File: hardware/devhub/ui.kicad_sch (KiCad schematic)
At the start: 12 parts, among them U10 74HC595, U11 74HC595

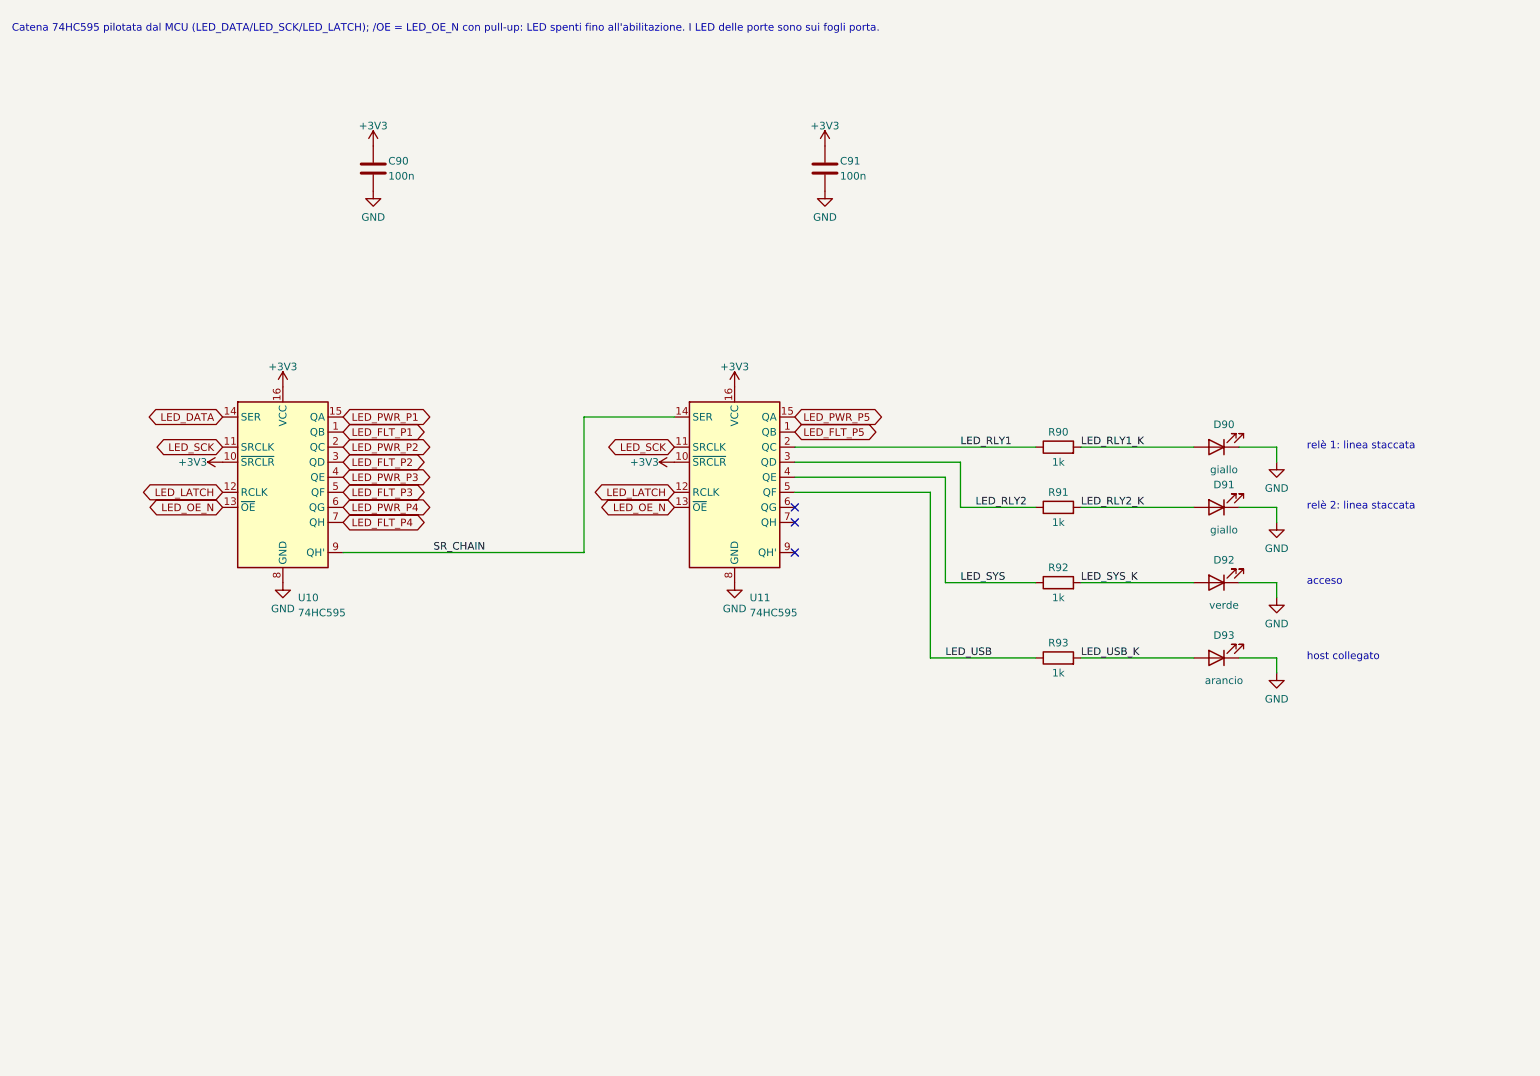
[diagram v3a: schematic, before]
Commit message: Simplification: drop the 74HC595s, green LEDs on port EN, relay LEDs on relay commands (D38)
Red port LEDs and the host LED are driven by GPIOs that stay low in DFU; the power LED is on 3.3 V.
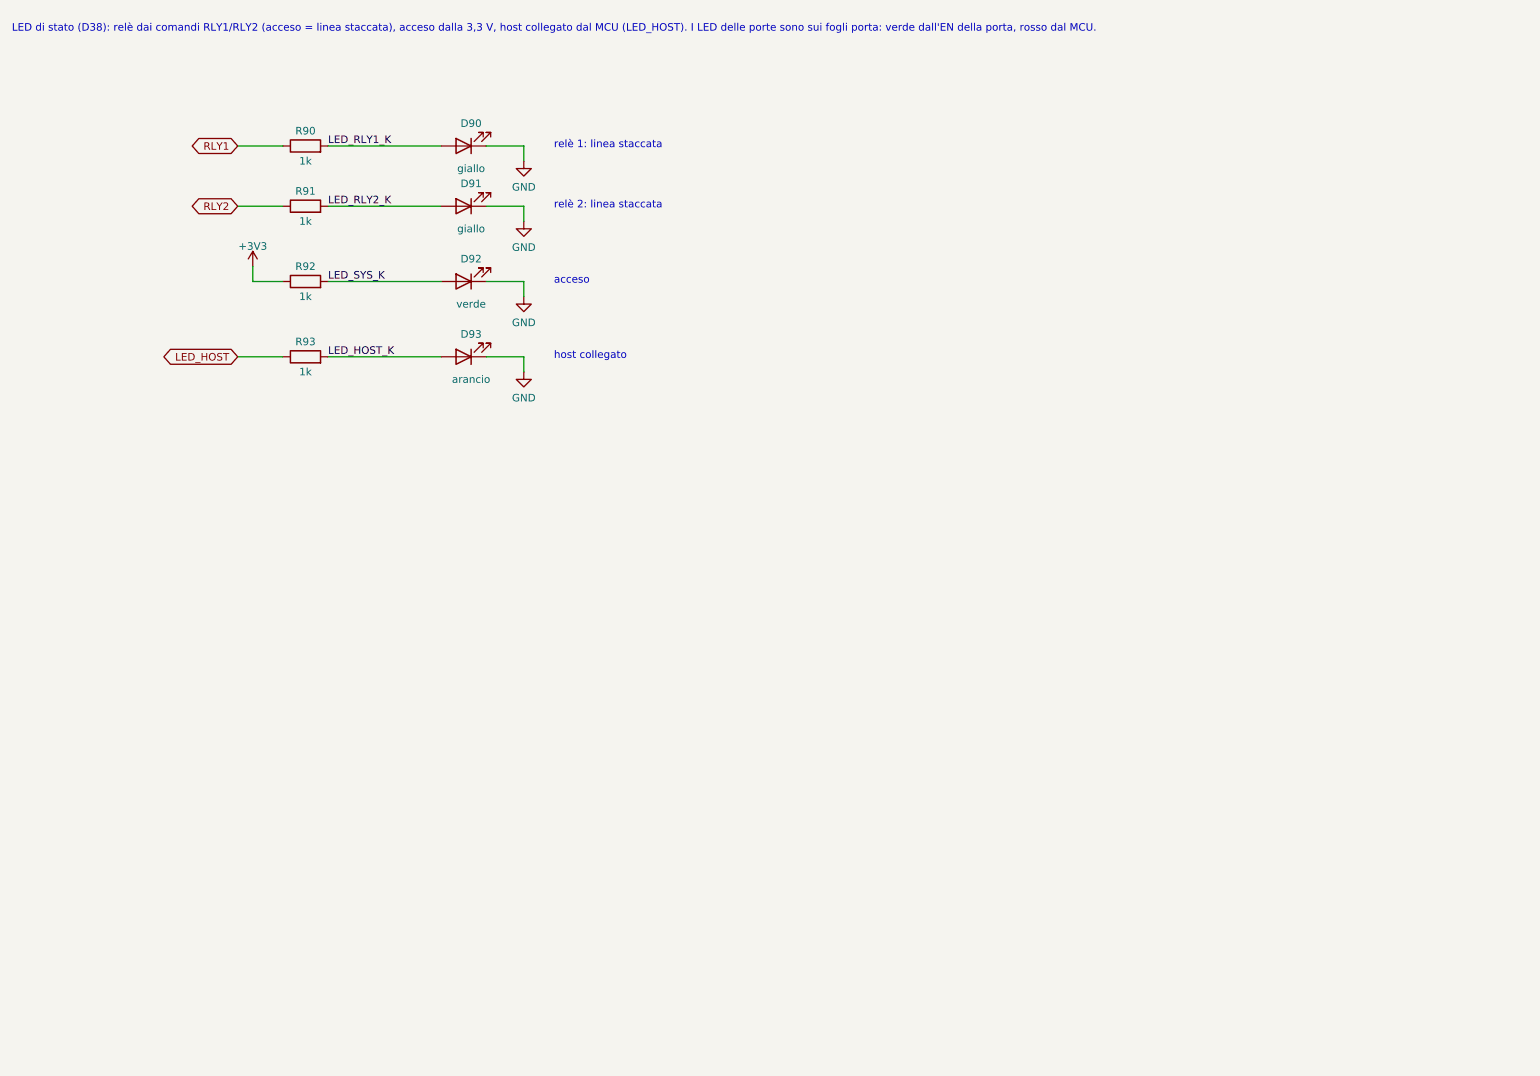
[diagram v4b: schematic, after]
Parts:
- removed C90, C91: 100n, Capacitor_SMD:C_0603_1608Metric, symbol Device:C
- removed U10, U11: 74HC595, Package_SO:SOIC-16_3.9x9.9mm_P1.27mm, symbol 74xx:74HC595
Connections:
- net LED_SYS is gone; now on net +3V3: R92.1
- net LED_RLY1 renamed RLY1
- net LED_RLY2 renamed RLY2
- net LED_USB renamed LED_HOST
- net LED_USB_K renamed LED_HOST_K
- no-connect marks 3 -> 0
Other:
- note added: "LED di stato (D38): relè dai comandi RLY1/RLY2 (acceso = linea staccata), acceso dalla 3,3 V, host collegato dal MCU (LED_HOST). I LED delle porte sono sui fogli porta: verde dall'EN della porta, rosso dal MCU."
- note removed: "Catena 74HC595 pilotata dal MCU (LED_DATA/LED_SCK/LED_LATCH); /OE = LED_OE_N con pull-up: LED spenti fino all'abilitazione. I LED delle porte sono sui fogli porta."
- title: LED di stato (74HC595 x2) -> LED di stato
- moved on the sheet: D90, D91, D92, D93, R90, R91, R92, R93

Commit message: Intial PCB layout
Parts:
- D90, D91: value giallo -> verde
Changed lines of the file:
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@@
 		(company "devhub")
+	)
+	(text "LED di stato (D38): relè dai comandi RLY1/RLY2 (acceso = linea staccata), acceso dalla 3,3 V, host collegato dal MCU (LED_HOST). I LED delle porte sono sui fogli porta: verde dall'EN della porta, rosso dal MCU."
+		(exclude_from_sim no)
+		(at 10.16 16.51 0)
+		(effects
+			(font
+				(size 1.27 1.27)
+			)
+			(justify left bottom)
+		)
 	)
 	(text "relè 1: linea staccata"
@@
 	(wire
 		(pts
+			(xy 48.26 35.56) (xy 55.88 35.56)
+		)
+		(stroke
+			(width 0)
+			(type default)
+		)
+	)
+	(wire
+		(pts
 			(xy 90.17 58.42) (xy 96.52 58.42)
 		)
@@
 	(wire
 		(pts
+			(xy 48.26 71.12) (xy 55.88 71.12)
+		)
+		(stroke
+			(width 0)
+			(type default)
+		)
+	)
+	(wire
+		(pts
 			(xy 96.52 71.12) (xy 96.52 73.66)
 		)
@@
 	(wire
 		(pts
+			(xy 48.26 45.72) (xy 55.88 45.72)
+		)
+		(stroke
+			(width 0)
+			(type default)
+		)
+	)
+	(wire
+		(pts
 			(xy 96.52 45.72) (xy 96.52 48.26)
+		)
+		(stroke
+			(width 0)
+			(type default)
+		)
+	)
+	(wire
+		(pts
+			(xy 50.8 58.42) (xy 55.88 58.42)
+		)
+		(stroke
+			(width 0)
+			(type default)
+		)
+	)
+	(wire
+		(pts
+			(xy 50.8 55.88) (xy 50.8 58.42)
 		)
 		(stroke
@@
 		)
 	)
-	(wire
-		(pts
-			(xy 48.26 35.56) (xy 55.88 35.56)
-		)
-		(stroke
-			(width 0)
-			(type default)
+	(global_label "LED_HOST"
+		(shape bidirectional)
+		(at 48.26 71.12 180)
+		(fields_autoplaced yes)
+		(effects
+			(font
+				(size 1.27 1.27)
+			)
+			(justify right)
+		)
+		(property "Intersheetrefs" "${INTERSHEET_REFS}"
+			(at 48.26 71.12 0)
+			(hide yes)
+			(show_name no)
+			(do_not_autoplace no)
+			(effects
+				(font
+					(size 1.27 1.27)
+				)
+			)
 		)
 	)
@@
 		)
 	)
-	(wire
-		(pts
-			(xy 48.26 45.72) (xy 55.88 45.72)
-		)
-		(stroke
-			(width 0)
-			(type default)
-		)
-	)
 	(global_label "RLY2"
 		(shape bidirectional)
@@
 		)
 	)
-	(wire
-		(pts
-			(xy 50.8 55.88) (xy 50.8 58.42)
-		)
-		(stroke
-			(width 0)
-			(type default)
-		)
-	)
-	(wire
-		(pts
-			(xy 50.8 58.42) (xy 55.88 58.42)
-		)
-		(stroke
-			(width 0)
-			(type default)
-		)
-	)
-	(wire
-		(pts
-			(xy 48.26 71.12) (xy 55.88 71.12)
-		)
-		(stroke
-			(width 0)
-			(type default)
-		)
-	)
-	(global_label "LED_HOST"
-		(shape bidirectional)
-		(at 48.26 71.12 180)
-		(fields_autoplaced yes)
-		(effects
-			(font
-				(size 1.27 1.27)
-			)
-			(justify right)
-		)
-		(property "Intersheetrefs" "${INTERSHEET_REFS}"
-			(at 48.26 71.12 0)
-			(hide yes)
-			(show_name no)
-			(do_not_autoplace no)
-			(effects
-				(font
-					(size 1.27 1.27)
-				)
-			)
-		)
-	)
-	(text "LED di stato (D38): relè dai comandi RLY1/RLY2 (acceso = linea staccata), acceso dalla 3,3 V, host collegato dal MCU (LED_HOST). I LED delle porte sono sui fogli porta: verde dall'EN della porta, rosso dal MCU."
-		(exclude_from_sim no)
-		(at 10.16 16.51 0)
-		(effects
-			(font
-				(size 1.27 1.27)
-			)
-			(justify left bottom)
-		)
-	)
 	(symbol
 		(lib_id "Device:LED")
@@
 			)
 		)
-		(property "Value" "giallo"
+		(property "Value" "verde"
 			(at 87.63 49.53 0)
 			(show_name no)
@@
 	)
 	(symbol
+		(lib_id "power:+3V3")
+		(at 50.8 55.88 0)
+		(unit 1)
+		(body_style 1)
+		(exclude_from_sim no)
+		(in_bom yes)
+		(on_board yes)
+		(in_pos_files yes)
+		(dnp no)
+		(property "Reference" "#PWR159"
+			(at 50.8 55.88 0)
+			(hide yes)
+			(show_name no)
+			(do_not_autoplace no)
+			(effects
+				(font
+					(size 1.27 1.27)
+				)
+			)
+		)
+		(property "Value" "+3V3"
+			(at 50.8 52.48 0)
+			(show_name no)
+			(do_not_autoplace no)
+			(effects
+				(font
+					(size 1.27 1.27)
+				)
+			)
+		)
+		(property "Footprint" ""
+			(at 50.8 55.88 0)
+			(hide yes)
+			(show_name no)
+			(do_not_autoplace no)
+			(effects
+				(font
+					(size 1.27 1.27)
+				)
+			)
+		)
+		(property "Datasheet" ""
+			(at 50.8 55.88 0)
+			(hide yes)
+			(show_name no)
+			(do_not_autoplace no)
+			(effects
+				(font
+					(size 1.27 1.27)
+				)
+			)
+		)
+		(property "Description" ""
+			(at 50.8 55.88 0)
+			(hide yes)
+			(show_name no)
+			(do_not_autoplace no)
+			(effects
+				(font
+					(size 1.27 1.27)
+				)
+			)
+		)
+		(pin "1"
+		)
+		(instances
+			(project "devhub"
+				(path "/af6ea7d8-d1ba-5fc6-aec8-abf514847630/c82dde94-3a77-5cb6-9c61-f280daabce7c"
+					(reference "#PWR159")
+					(unit 1)
+				)
+			)
+		)
+	)
+	(symbol
 		(lib_id "power:GND")
 		(at 96.52 73.66 0)
@@
 			)
 		)
-		(property "Value" "giallo"
+		(property "Value" "verde"
 			(at 87.63 39.37 0)
 			(show_name no)
@@
 					(unit 1)
 				)
-			)
-		)
-	)
-	(symbol
-		(lib_id "power:+3V3")
-		(at 50.8 55.88 0)
-		(unit 1)
-		(body_style 1)
-		(exclude_from_sim no)
-		(in_bom yes)
-		(on_board yes)
-		(in_pos_files yes)
-		(dnp no)
-		(property "Reference" "#PWR159"
-			(at 50.8 55.88 0)
-			(hide yes)
-			(show_name no)
-			(do_not_autoplace no)
-			(effects
-				(font
-					(size 1.27 1.27)
-				)
-			)
-		)
-		(property "Value" "+3V3"
-			(at 50.8 52.48 0)
-			(show_name no)
-			(do_not_autoplace no)
-			(effects
-				(font
-					(size 1.27 1.27)
-				)
-			)
-		)
-		(property "Footprint" ""
-			(at 50.8 55.88 0)
-			(hide yes)
-			(show_name no)
-			(do_not_autoplace no)
-			(effects
-				(font
-					(size 1.27 1.27)
-				)
-			)
-		)
-		(property "Datasheet" ""
-			(at 50.8 55.88 0)
-			(hide yes)
-			(show_name no)
-			(do_not_autoplace no)
-			(effects
-				(font
-					(size 1.27 1.27)
-				)
-			)
-		)
-		(property "Description" ""
-			(at 50.8 55.88 0)
-			(hide yes)
-			(show_name no)
-			(do_not_autoplace no)
-			(effects
-				(font
-					(size 1.27 1.27)
-				)
-			)
-		)
-		(pin "1"
-		)
-		(instances
-			(project "devhub"
-				(path "/af6ea7d8-d1ba-5fc6-aec8-abf514847630/c82dde94-3a77-5cb6-9c61-f280daabce7c"
-					(reference "#PWR159")
-					(unit 1)
-				)

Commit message: PCB rules in KiCad, USB pair names, eFuse output bypass and U2 thermal vias (D44-D50)
Stackup JLC04161H-7628, netclasses and custom DRC rules (devhub.kicad_dru) from
docs/regole-pcb.md, with a section for the checks that DRC cannot cover. C7 1 uF on
the TPS259470A output before the shunt (D48). USB nets renamed to DP/DN so KiCad
recognizes the differential pairs (D49). U2 footprint with 0.3 mm thermal vias, open
on both sides for the prototype; encroached vias and a JLCPCB order note for
production (D50). Also includes stock part codes, cost comparison and placement rules
(D44-D47).
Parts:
- D90, D91, D92: digikey (none) -> 160-1423-1-ND; lcsc (none) -> C913075; mouser (none) -> 859-LTST-C171GKT
- D93: digikey (none) -> 160-1425-1-ND; lcsc (none) -> C284932; mouser (none) -> 859-LTST-C171KFKT
- R90, R91, R92, R93: digikey (none) -> 311-1.00KHRCT-ND; lcsc (none) -> C21190; mouser (none) -> 603-RC0603FR-071KL; warehouse (none) -> 284

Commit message: Schematic v0.3: apply simplified requirements (D79-D81)
Update the existing KiCad project instead of starting over:
- MCU U3 replaced with STM32G0B1CEU6 (UFQFPN48) on the 48-pin pinout
- switches sheet: two UCS2114-1-V/LX on separate I2C buses replace
  TPS2561A, INA3221 and current shunts
- ports: single MCU-driven LED, discrete VBUS discharge removed
- remove USB-A port, spare hub header, second relay channel,
  input CC ADC filters and input shunt
- add UCS2114 symbol and footprint (Microchip land pattern C04-2421)
- align pinout, decisions, architecture and component docs
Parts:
- removed D91: verde, LED_SMD:LED_0805_2012Metric, symbol Device:LED
- removed R91: 1k, Resistor_SMD:R_0603_1608Metric, symbol Device:R
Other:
- note added: "LED di stato: relè dal comando RLY1 (acceso = linea staccata), acceso dalla 3,3 V, host collegato dal MCU (LED_HOST). Il LED di ogni porta è nel foglio porta, pilotato dal MCU (D63)."
- note added: "relè: linea staccata"
- note removed: "LED di stato (D38): relè dai comandi RLY1/RLY2 (acceso = linea staccata), acceso dalla 3,3 V, host collegato dal MCU (LED_HOST). I LED delle porte sono sui fogli porta: verde dall'EN della porta, rosso dal MCU."
- note removed: "relè 1: linea staccata"
- note removed: "relè 2: linea staccata"
